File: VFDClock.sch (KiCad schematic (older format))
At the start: 21 parts, among them J1 Barrel_Jack_MountingPin, P1 Power, P2 Analog, P3 Digital, P4 Digital, Q1 VFD_LD8035E, Q2 VFD_LD8035E, Q3 VFD_LD8035E, Q4 VFD_LD8035E, Q5 VFD_LD8035E, Q6 VFD_LD8035E, U1 IC_HT16K33

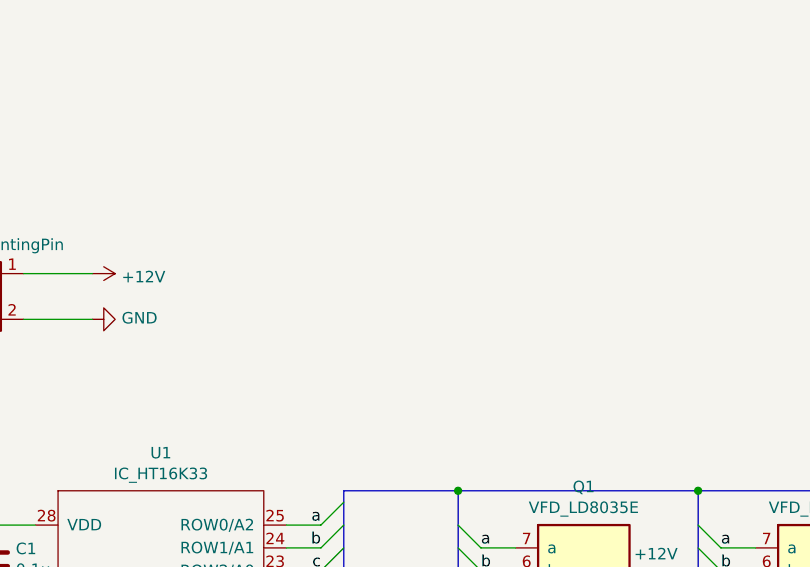
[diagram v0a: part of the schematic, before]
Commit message: RTCを追加
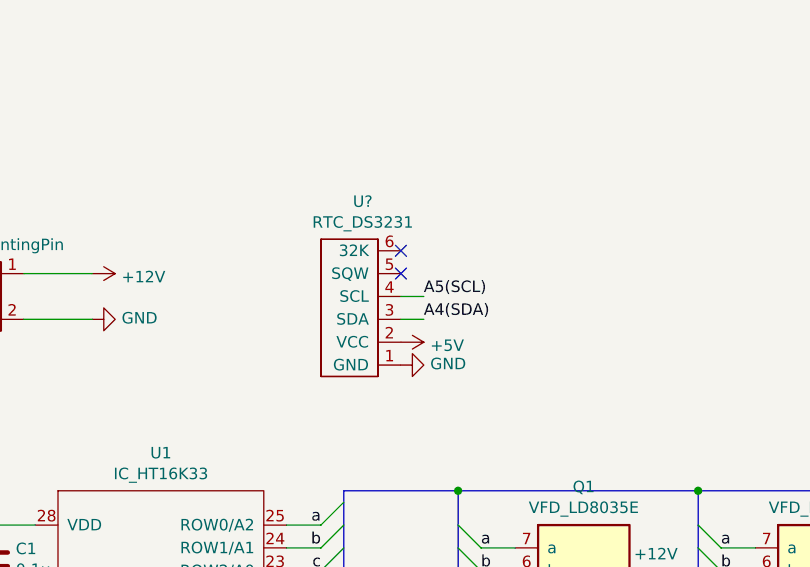
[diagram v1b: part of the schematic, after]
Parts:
- added U?: RTC_DS3231, symbol MyParts:RTC_DS3231
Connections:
- net +5V: now also U?.2 (VCC)
- net A4(SDA): now also U?.3 (SDA)
- net A5(SCL): now also U?.4 (SCL)
- net GND: now also U?.1 (GND)
- no-connect marks 42 -> 44
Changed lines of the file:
@@
 NoConn ~ 9400 2900
 NoConn ~ 9400 3000
+$Comp
+L MyParts:RTC_DS3231 U?
+U 1 1 5F2CBB77
+P 3350 3150
+F 0 "U?" V 3815 3167 50  0000 C CNN
+F 1 "RTC_DS3231" V 3724 3167 50  0000 C CNN
+F 2 "" H 3350 3500 50  0001 C CNN
+F 3 "" H 3350 3500 50  0001 C CNN
+	1    3350 3150
+	0    -1   -1   0
+$EndComp
+$Comp
+L power:GND #PWR?
+U 1 1 5F2CDC62
+P 3500 3400
+F 0 "#PWR?" H 3500 3150 50  0001 C CNN
+F 1 "GND" V 3505 3272 50  0000 R CNN
+F 2 "" H 3500 3400 50  0001 C CNN
+F 3 "" H 3500 3400 50  0001 C CNN
+	1    3500 3400
+	0    -1   -1   0
+$EndComp
+$Comp
+L power:+5V #PWR?
+U 1 1 5F2CEAC2
+P 3500 3300
+F 0 "#PWR?" H 3500 3150 50  0001 C CNN
+F 1 "+5V" V 3515 3428 50  0000 L CNN
+F 2 "" H 3500 3300 50  0001 C CNN
+F 3 "" H 3500 3300 50  0001 C CNN
+	1    3500 3300
+	0    1    1    0
+$EndComp
+Wire Wire Line
+	3500 3200 3600 3200
+Wire Wire Line
+	3500 3100 3600 3100
+NoConn ~ 3500 3000
+NoConn ~ 3500 2900
 Wire Bus Line
 	9150 3950 9150 4900
@@
 Wire Bus Line
 	3750 3950 3750 4900
+Text Label 3600 3200 0    50   ~ 0
+A4(SDA)
+Text Label 3600 3100 0    50   ~ 0
+A5(SCL)
 $EndSCHEMATC

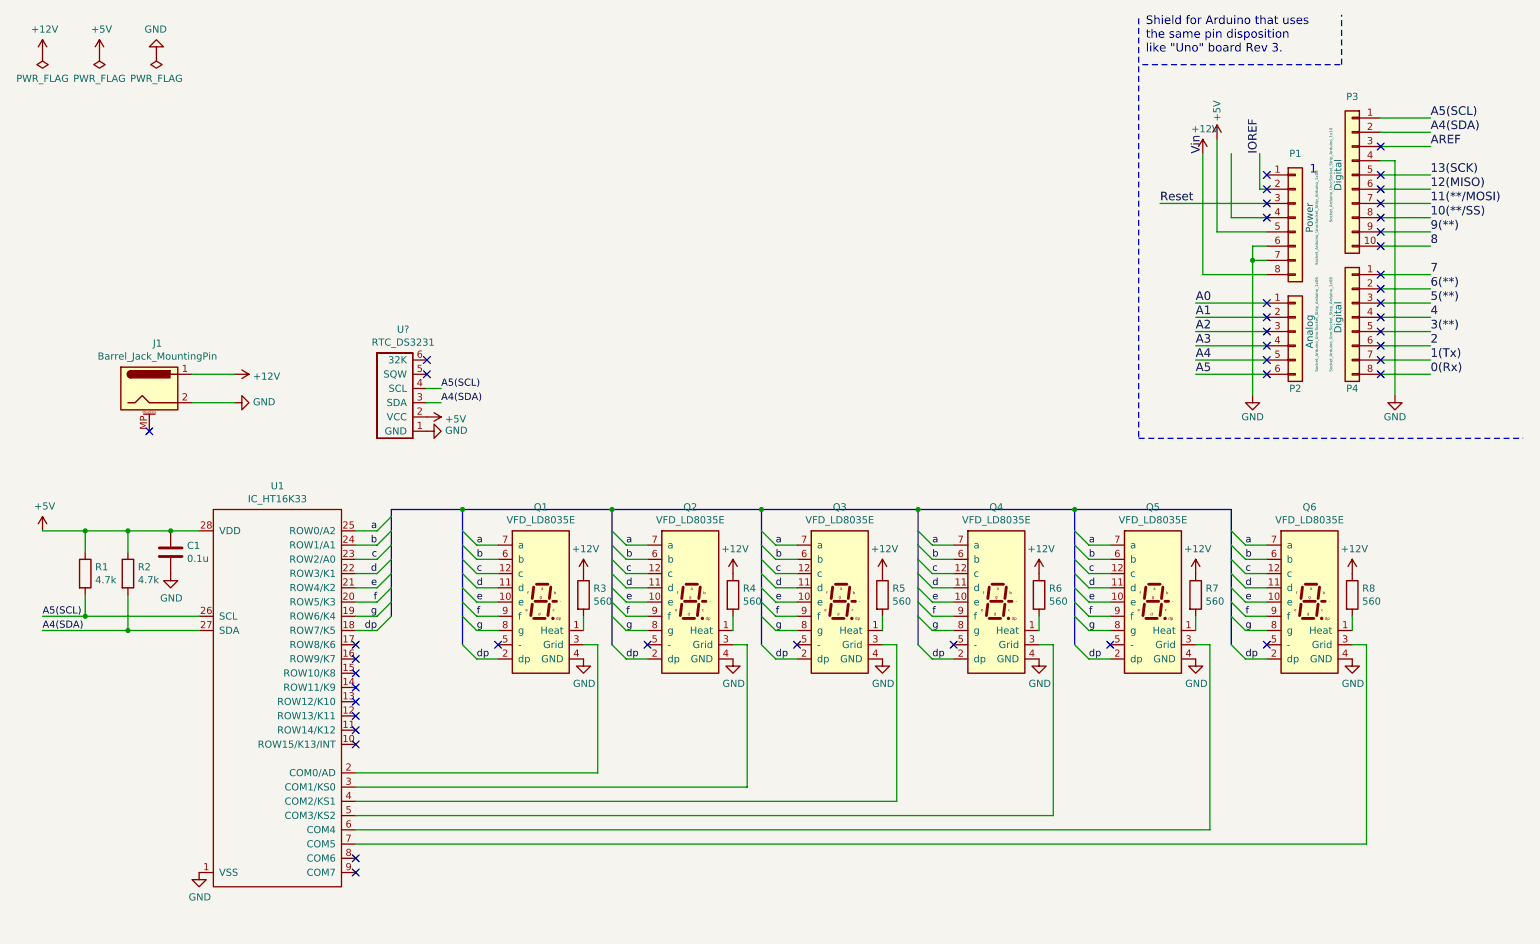
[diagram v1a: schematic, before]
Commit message: 駆動用トランジスタアレイを追加
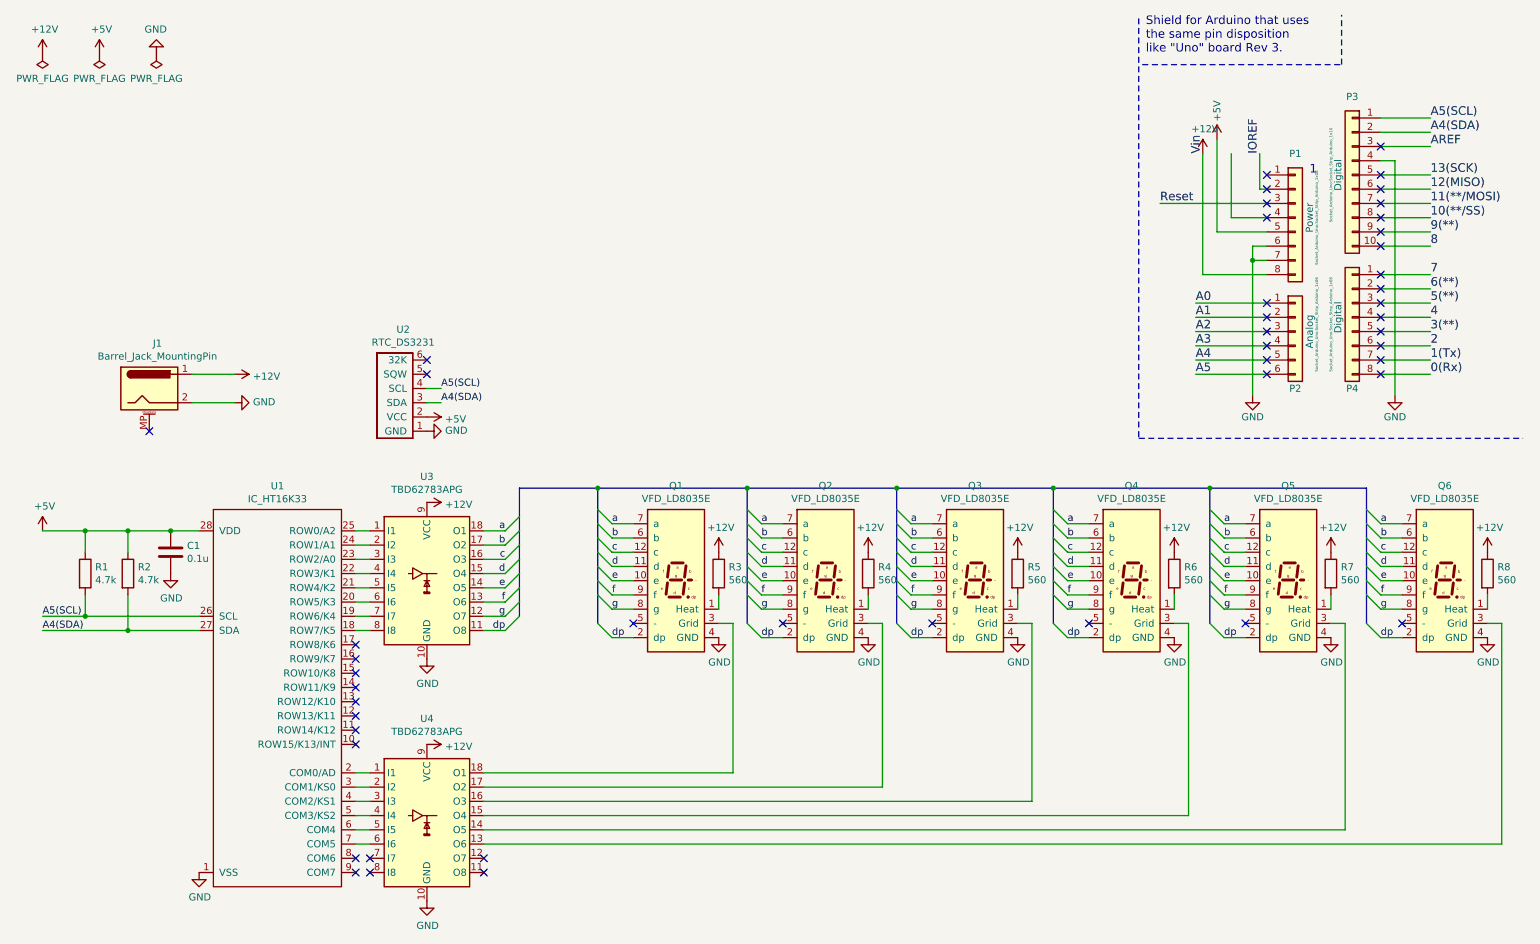
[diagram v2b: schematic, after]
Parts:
- added U3, U4: TBD62783APG, symbol Transistor_Array:TBD62783A
- gave numbers to parts that had none: 1
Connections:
- net +12V: now also U3.9 (VCC), U4.9 (VCC)
- net GND: now also U3.10 (GND), U4.10 (GND)
- net a: now also U3.18 (O1); no longer U1.25 (ROW0/A2)
- net b: now also U3.17 (O2); no longer U1.24 (ROW1/A1)
- net c: now also U3.16 (O3); no longer U1.23 (ROW2/A0)
- net d: now also U3.15 (O4); no longer U1.22 (ROW3/K1)
- net dp: now also U3.11 (O8); no longer U1.18 (ROW7/K5)
- net e: now also U3.14 (O5); no longer U1.21 (ROW4/K2)
- net f: now also U3.13 (O6); no longer U1.20 (ROW5/K3)
- net g: now also U3.12 (O7); no longer U1.19 (ROW6/K4)
- net at U1.2 (COM0/AD): now also U4.1 (I1); no longer Q1.3 (Grid)
- net at U1.3 (COM1/KS0): now also U4.2 (I2); no longer Q2.3 (Grid)
- net at U1.4 (COM2/KS1): now also U4.3 (I3); no longer Q3.3 (Grid)
- net at U1.5 (COM3/KS2): now also U4.4 (I4); no longer Q4.3 (Grid)
- net at U1.6 (COM4): now also U4.5 (I5); no longer Q5.3 (Grid)
- net at U1.7 (COM5): now also U4.6 (I6); no longer Q6.3 (Grid)
- new net: U1.18 (ROW7/K5), U3.8 (I8)
- new net: U1.19 (ROW6/K4), U3.7 (I7)
- new net: U1.20 (ROW5/K3), U3.6 (I6)
- new net: U1.21 (ROW4/K2), U3.5 (I5)
- new net: U1.22 (ROW3/K1), U3.4 (I4)
- new net: U1.23 (ROW2/A0), U3.3 (I3)
- new net: U1.24 (ROW1/A1), U3.2 (I2)
- new net: U1.25 (ROW0/A2), U3.1 (I1)
- new net: Q1.3 (Grid), U4.18 (O1)
- new net: Q2.3 (Grid), U4.17 (O2)
- new net: Q3.3 (Grid), U4.16 (O3)
- new net: Q4.3 (Grid), U4.15 (O4)
- new net: Q6.3 (Grid), U4.13 (O6)
- new net: Q5.3 (Grid), U4.14 (O5)
- no-connect marks 44 -> 48
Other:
- moved on the sheet: Q1, Q2, Q3, Q4, Q5, Q6, R3, R4, R5, R6, R7, R8

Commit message: 抵抗値を変更
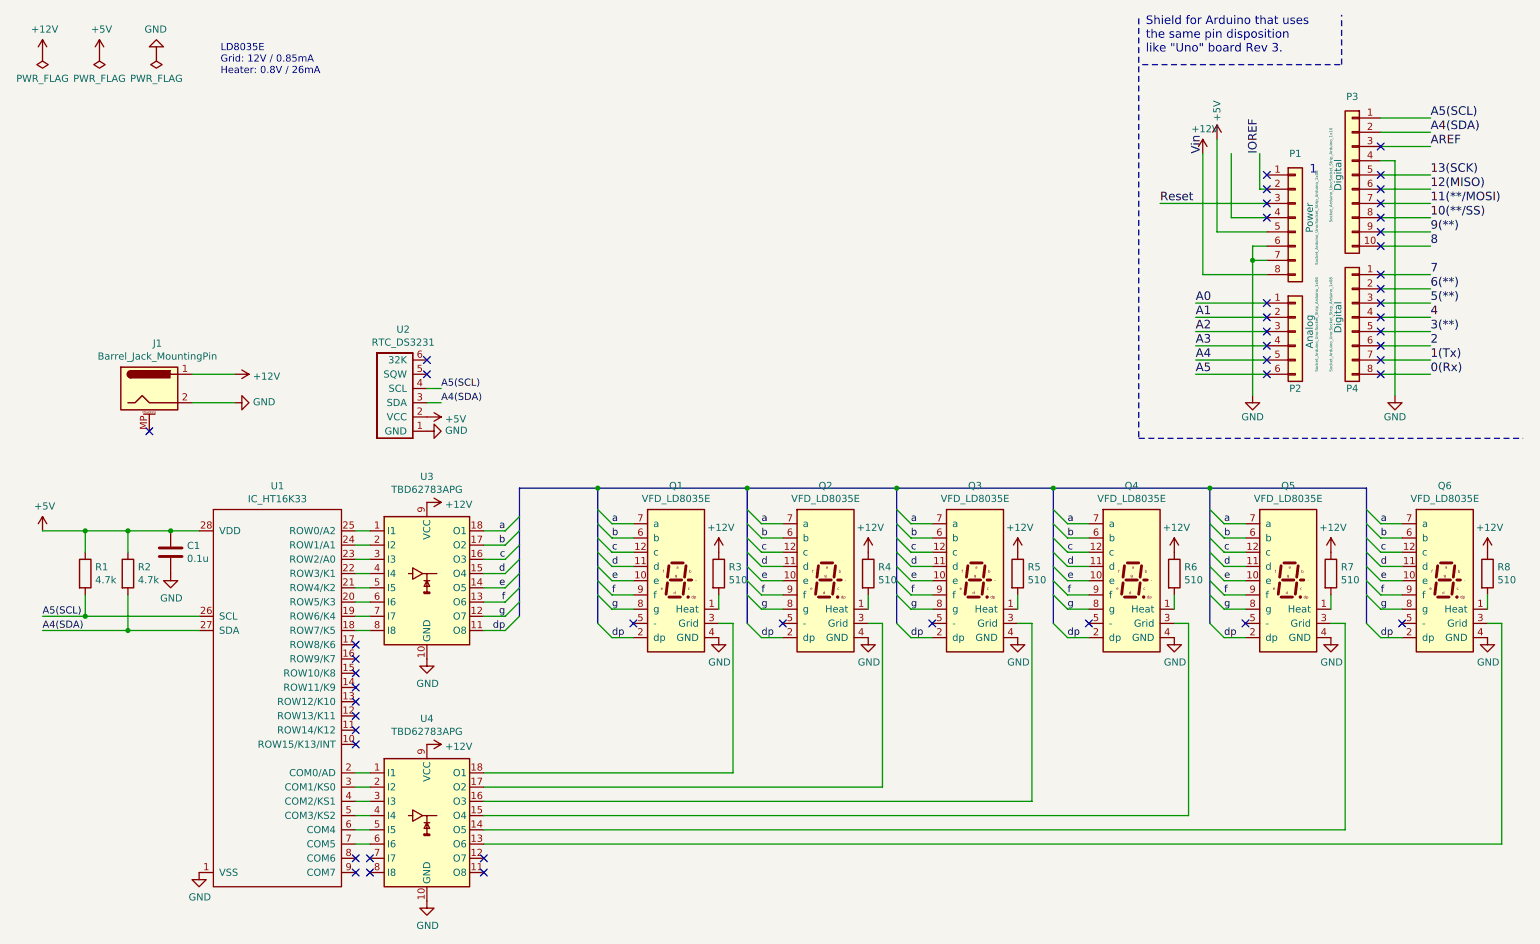
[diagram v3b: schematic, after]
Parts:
- R3, R4, R5, R6, R7, R8: value 560 -> 510
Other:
- note added: "LD8035E\nGrid: 12V / 0.85mA\nHeater: 0.8V / 26mA"
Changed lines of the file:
@@
 P 5550 4400
 F 0 "R3" H 5620 4446 50  0000 L CNN
-F 1 "560" H 5620 4355 50  0000 L CNN
+F 1 "510" H 5620 4355 50  0000 L CNN
 F 2 "Resistor_THT:R_Axial_DIN0207_L6.3mm_D2.5mm_P7.62mm_Horizontal" V 5480 4400 50  0001 C CNN
 F 3 "~" H 5550 4400 50  0001 C CNN
@@
 P 6600 4400
 F 0 "R4" H 6670 4446 50  0000 L CNN
-F 1 "560" H 6670 4355 50  0000 L CNN
+F 1 "510" H 6670 4355 50  0000 L CNN
 F 2 "Resistor_THT:R_Axial_DIN0207_L6.3mm_D2.5mm_P7.62mm_Horizontal" V 6530 4400 50  0001 C CNN
 F 3 "~" H 6600 4400 50  0001 C CNN
@@
 P 7650 4400
 F 0 "R5" H 7720 4446 50  0000 L CNN
-F 1 "560" H 7720 4355 50  0000 L CNN
+F 1 "510" H 7720 4355 50  0000 L CNN
 F 2 "Resistor_THT:R_Axial_DIN0207_L6.3mm_D2.5mm_P7.62mm_Horizontal" V 7580 4400 50  0001 C CNN
 F 3 "~" H 7650 4400 50  0001 C CNN
@@
 P 8750 4400
 F 0 "R6" H 8820 4446 50  0000 L CNN
-F 1 "560" H 8820 4355 50  0000 L CNN
+F 1 "510" H 8820 4355 50  0000 L CNN
 F 2 "Resistor_THT:R_Axial_DIN0207_L6.3mm_D2.5mm_P7.62mm_Horizontal" V 8680 4400 50  0001 C CNN
 F 3 "~" H 8750 4400 50  0001 C CNN
@@
 P 9850 4400
 F 0 "R7" H 9920 4446 50  0000 L CNN
-F 1 "560" H 9920 4355 50  0000 L CNN
+F 1 "510" H 9920 4355 50  0000 L CNN
 F 2 "Resistor_THT:R_Axial_DIN0207_L6.3mm_D2.5mm_P7.62mm_Horizontal" V 9780 4400 50  0001 C CNN
 F 3 "~" H 9850 4400 50  0001 C CNN
@@
 P 10950 4400
 F 0 "R8" H 11020 4446 50  0000 L CNN
-F 1 "560" H 11020 4355 50  0000 L CNN
+F 1 "510" H 11020 4355 50  0000 L CNN
 F 2 "Resistor_THT:R_Axial_DIN0207_L6.3mm_D2.5mm_P7.62mm_Horizontal" V 10880 4400 50  0001 C CNN
 F 3 "~" H 10950 4400 50  0001 C CNN
@@
 NoConn ~ 3900 6400
 NoConn ~ 3900 6500
+Text Notes 2050 900  0    50   ~ 0
+LD8035E\nGrid: 12V / 0.85mA\nHeater: 0.8V / 26mA
 Wire Bus Line
 	10100 3800 10100 4750

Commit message: フットプリントの関連付けを更新
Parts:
- U2: footprint (none) -> #MyFootPrints:RTC_DS3231_Vertical
- U3, U4: footprint (none) -> Package_DIP:DIP-18_W7.62mm
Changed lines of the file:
@@
 F 0 "U2" V 3815 3167 50  0000 C CNN
 F 1 "RTC_DS3231" V 3724 3167 50  0000 C CNN
-F 2 "" H 3350 3500 50  0001 C CNN
+F 2 "#MyFootPrints:RTC_DS3231_Vertical" H 3350 3500 50  0001 C CNN
 F 3 "" H 3350 3500 50  0001 C CNN
 	1    3350 3150
@@
 F 0 "U3" H 3500 5081 50  0000 C CNN
 F 1 "TBD62783APG" H 3500 4990 50  0000 C CNN
-F 2 "" H 3500 3850 50  0001 C CNN
+F 2 "Package_DIP:DIP-18_W7.62mm" H 3500 3850 50  0001 C CNN
 F 3 "http://toshiba.semicon-storage.com/info/docget.jsp?did=30523&prodName=TBD62783APG" H 3200 4800 50  0001 C CNN
 	1    3500 4400
@@
 F 0 "U4" H 3500 6781 50  0000 C CNN
 F 1 "TBD62783APG" H 3500 6690 50  0000 C CNN
-F 2 "" H 3500 5550 50  0001 C CNN
+F 2 "Package_DIP:DIP-18_W7.62mm" H 3500 5550 50  0001 C CNN
 F 3 "http://toshiba.semicon-storage.com/info/docget.jsp?did=30523&prodName=TBD62783APG" H 3200 6500 50  0001 C CNN
 	1    3500 6100

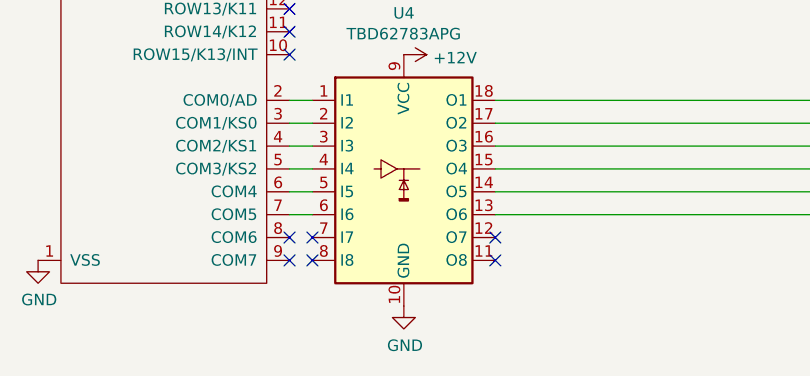
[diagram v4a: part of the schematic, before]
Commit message: 未使用ピンの処理
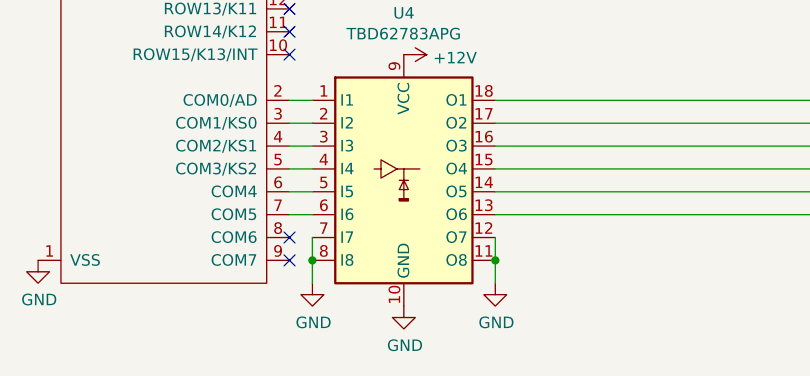
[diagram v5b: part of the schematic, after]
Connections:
- net GND: now also U4.11 (O8), U4.12 (O7), U4.7 (I7), U4.8 (I8)
- no-connect marks 48 -> 44
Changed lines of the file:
@@
 	0    1    1    0
-$EndComp
-$Comp
-L Transistor_Array:TBD62783A U4
-U 1 1 5F2B7001
-P 3500 6100
-F 0 "U4" H 3500 6781 50  0000 C CNN
-F 1 "TBD62783APG" H 3500 6690 50  0000 C CNN
-F 2 "Package_DIP:DIP-18_W7.62mm" H 3500 5550 50  0001 C CNN
-F 3 "http://toshiba.semicon-storage.com/info/docget.jsp?did=30523&prodName=TBD62783APG" H 3200 6500 50  0001 C CNN
-	1    3500 6100
-	1    0    0    -1
 $EndComp
 Wire Wire Line
@@
 Wire Wire Line
 	3900 5900 6700 5900
-NoConn ~ 3100 6400
-NoConn ~ 3100 6500
 $Comp
 L power:GND #PWR0119
@@
 	0    1    1    0
 $EndComp
-NoConn ~ 3900 6400
-NoConn ~ 3900 6500
 Text Notes 2050 900  0    50   ~ 0
 LD8035E\nGrid: 12V / 0.85mA\nHeater: 0.8V / 26mA
+$Comp
+L Transistor_Array:TBD62783A U4
+U 1 1 5F2B7001
+P 3500 6100
+F 0 "U4" H 3500 6781 50  0000 C CNN
+F 1 "TBD62783APG" H 3500 6690 50  0000 C CNN
+F 2 "Package_DIP:DIP-18_W7.62mm" H 3500 5550 50  0001 C CNN
+F 3 "http://toshiba.semicon-storage.com/info/docget.jsp?did=30523&prodName=TBD62783APG" H 3200 6500 50  0001 C CNN
+	1    3500 6100
+	1    0    0    -1
+$EndComp
+$Comp
+L power:GND #PWR?
+U 1 1 5F215EAA
+P 3100 6600
+F 0 "#PWR?" H 3100 6350 50  0001 C CNN
+F 1 "GND" H 3105 6427 50  0000 C CNN
+F 2 "" H 3100 6600 50  0001 C CNN
+F 3 "" H 3100 6600 50  0001 C CNN
+	1    3100 6600
+	1    0    0    -1
+$EndComp
+Wire Wire Line
+	3100 6400 3100 6500
+Connection ~ 3100 6500
+Wire Wire Line
+	3100 6500 3100 6600
+$Comp
+L power:GND #PWR?
+U 1 1 5F22AE7A
+P 3900 6600
+F 0 "#PWR?" H 3900 6350 50  0001 C CNN
+F 1 "GND" H 3905 6427 50  0000 C CNN
+F 2 "" H 3900 6600 50  0001 C CNN
+F 3 "" H 3900 6600 50  0001 C CNN
+	1    3900 6600
+	1    0    0    -1
+$EndComp
+Wire Wire Line
+	3900 6400 3900 6500
 Wire Bus Line
 	10100 3800 10100 4750
@@
 Wire Bus Line
 	4700 3800 4700 4750
+Connection ~ 3900 6500
+Wire Wire Line
+	3900 6500 3900 6600
 $EndSCHEMATC
